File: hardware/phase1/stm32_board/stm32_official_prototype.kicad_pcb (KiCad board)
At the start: 6 copper layers, 77 parts, among them CN11 Conn_02x36_Odd_Even, CN12 Conn_02x36_Odd_Even, CN14 USB_B_Micro, CN5 Conn_ARM_JTAG_SWD_10, T2 9013, U11 STM32L496ZGTx, U13 USBLC6-2SC6, U8 TSV631AILT, U9 ESDALC6V1W5

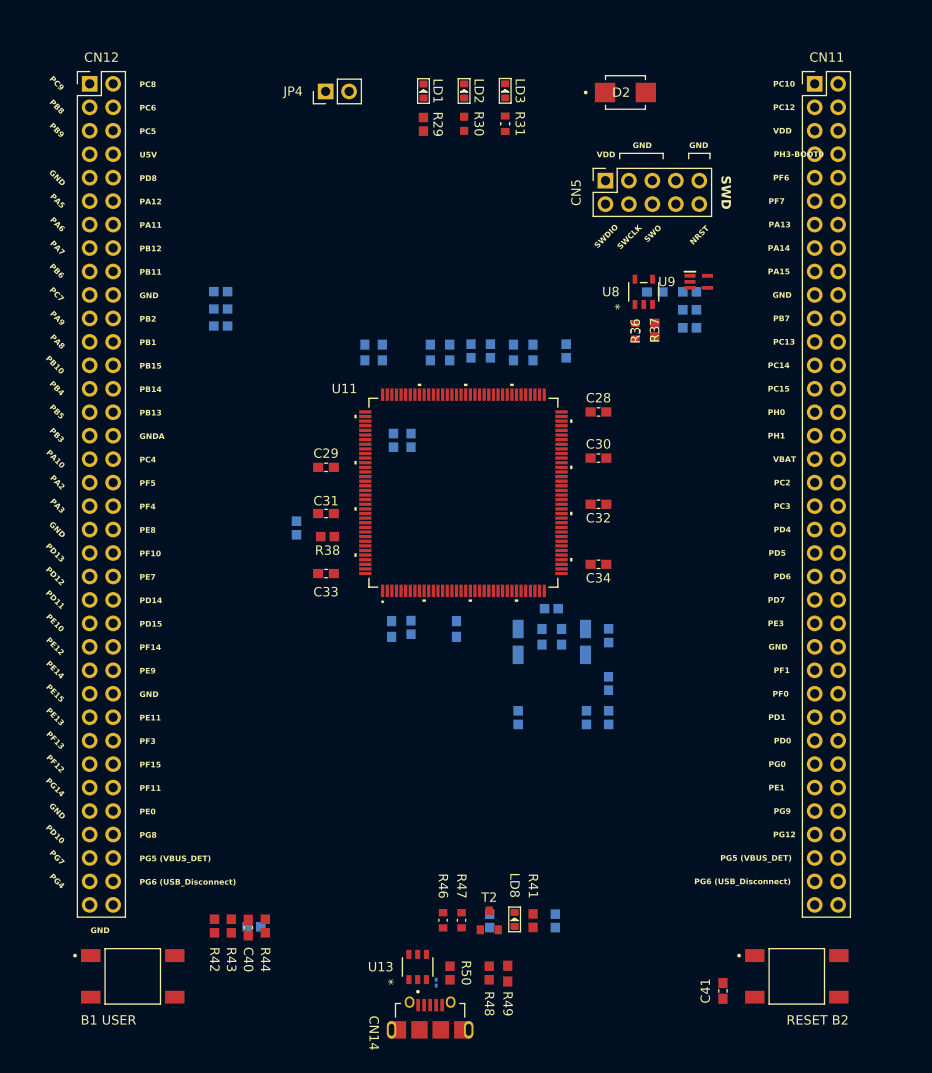
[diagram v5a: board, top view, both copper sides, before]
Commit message: toreyin meeting stm32 board update (1.29.25)
- I MUST NOT FORGET DIFFERENTIAL ROUTING FOR USB
- i need like 10 pins to wire, difficult at this point to get through the entire spider web of traces
- buttons, USB, LEDs, and power network need to be connected to main circuit
- we for sure ordering this week
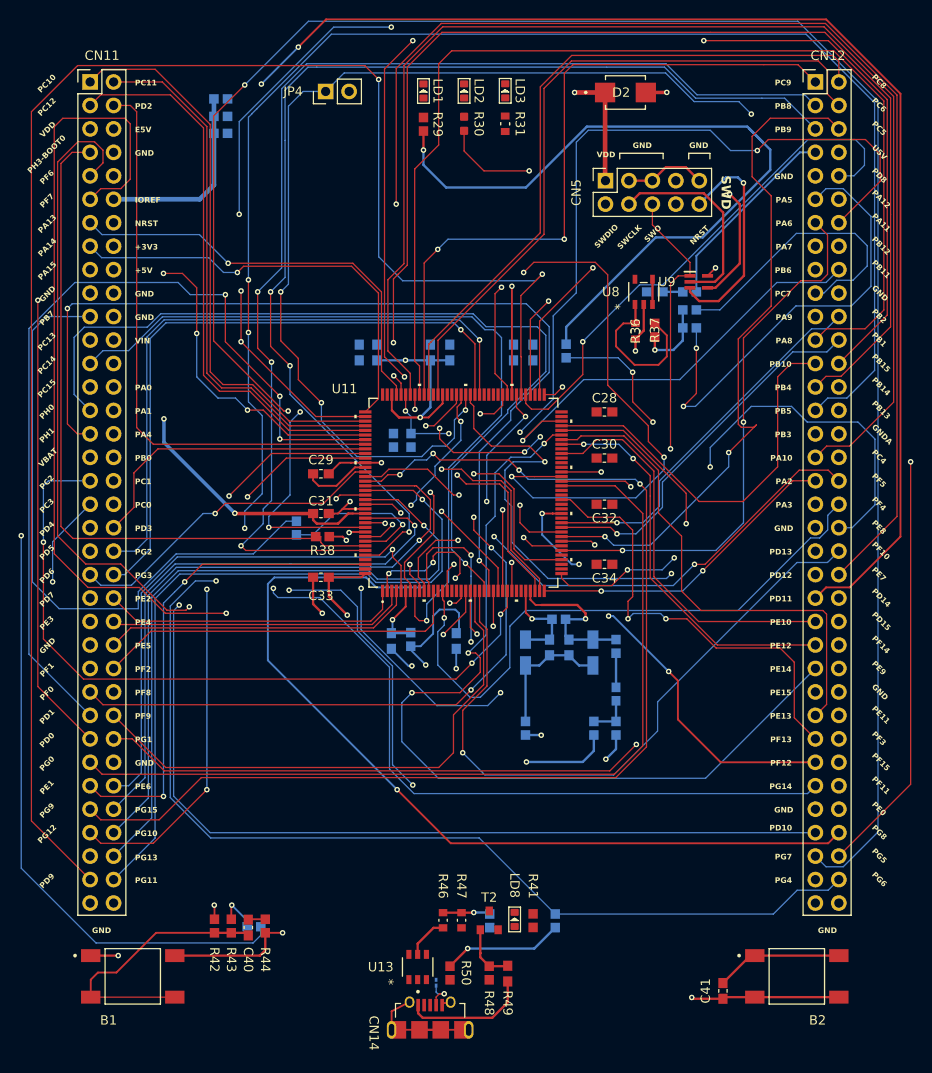
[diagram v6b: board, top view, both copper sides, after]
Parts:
- removed SB130, SB131: Closed, RC0603JR-070RL:RESC1607X60N
- B1: renamed from B1 USER
- B2: renamed from RESET B2
- moved CN12 78.6 mm to (171.4, 38.3)
- moved CN11 78.5 mm to (92.5, 38.3)
- moved SB111 20.9 mm to (103.6, 43.8)
- moved SB110 20.9 mm to (103.6, 40.1)
- moved SB112 20.9 mm to (103.6, 42.0)
- moved C58 1.40 mm to (141.3, 99.5)
- moved SB152 1.40 mm to (146.4, 99.4)
- moved SB158 1.40 mm to (144.0, 108.2)
- moved SB167 1.40 mm to (146.4, 108.2)
- moved C59 1.40 mm to (143.9, 100.0)
- moved L3 1.40 mm to (146.4, 104.5)
- moved C57 1.40 mm to (139.2, 99.5)
- moved SB149 1.40 mm to (140.2, 96.5)
- moved SB166 1.40 mm to (136.6, 108.2)
- moved C56 1.40 mm to (136.6, 100.0)
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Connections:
- R30 pad 1: Net-(R30-Pad1) -> PB7
- SB172 pad 1: PB7 -> Net-(U11-PB7)
- SB172 pad 2: Net-(R30-Pad1) -> PB7
- U11 pad 137: PB7 -> Net-(U11-PB7)
- U9 pad 5: (no net) -> GND
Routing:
- net PG7: track 0.00 -> 224.1 mm, vias 0 -> 3
- net VDD: track 0.00 -> 223.4 mm, vias 0 -> 6
- net PG5 (VBUS_DET): track 0.00 -> 208.0 mm, vias 0 -> 5
- net PE7: track 0.00 -> 204.6 mm, vias 0 -> 4
- net PD12: track 0.00 -> 193.4 mm, vias 0 -> 3
- net PD11: track 0.00 -> 188.4 mm, vias 0 -> 3
- net PD9: track 0.00 -> 178.4 mm, vias 0 -> 2
- net NRST: track 0.00 -> 176.5 mm, vias 0 -> 2
- net PB5: track 0.00 -> 171.0 mm, vias 0 -> 4
- net PD13: track 0.00 -> 166.2 mm, vias 0 -> 3
- net PB4: track 0.00 -> 162.1 mm, vias 0 -> 3
- net PB3: track 0.00 -> 157.2 mm, vias 0 -> 4
- net PG6 (USB_Disconnect): track 0.00 -> 149.1 mm, vias 0 -> 3
- net PD10: track 0.00 -> 146.7 mm, vias 0 -> 3
- net PC13: track 0.00 -> 146.0 mm, vias 0 -> 2
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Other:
- board text added: "+3V3"
- board text added: "+5V"
- board text added: "E5V"
- board text added: "IOREF"
- board text added: "PA0"
- board text added: "PA1"
- board text added: "PA4"
- board text added: "PB0"
- board text added: "PC0"
- board text added: "PC1"
- board text added: "PC11"
- board text added: "PD2"
- board text added: "PD3"
- board text added: "PD9"
- board text added: "PE2"
- board text added: "PE4"
- board text added: "PE5"
- board text added: "PE6"
- board text added: "PF2"
- board text added: "PF8"
- board text added: "PF9"
- board text added: "PG1"
- board text added: "PG10"
- board text added: "PG11"
- board text added: "PG13"
- board text added: "PG15"
- board text added: "PG2"
- board text added: "PG3"
- board text added: "PG5"
- board text added: "PG6"
- board text added: "VIN"
- board text removed: "PG5 (VBUS_DET)"
- board text removed: "PG6 (USB_Disconnect)"

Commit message: stm32 board update (2.2.25)
all...144 pins...are wired.
- still need to connect power circuitry to chip
- still need to connect USB circuitry to chip
- run by Mark Bruno tmrw --> order right away after
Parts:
- moved C30 0.50 mm to (145.2, 79.5)
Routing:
- net PD15: track 0.00 -> 135.5 mm, vias 0 -> 4
- net PD14: track 0.00 -> 132.1 mm, vias 0 -> 3
- net PE0: track 0.00 -> 96.0 mm, vias 0 -> 1
- net PF3: track 0.00 -> 75.9 mm, vias 0 -> 1
- net PF14: track 0.00 -> 66.9 mm, vias 0 -> 2
- net PF15: track 0.00 -> 66.2 mm, vias 0 -> 4
- net PE11: track 0.00 -> 56.4 mm
- net PF11: track 0.00 -> 55.6 mm, vias 0 -> 2
- net PE9: track 0.00 -> 50.0 mm, vias 0 -> 4
- net PG8: track 96.3 -> 126.2 mm, vias 1 -> 2
- net VDD_MCU: track 49.5 -> 57.2 mm
- net PG4: track 95.6 -> 101.9 mm
- net PE13: track 54.5 -> 60.8 mm
- net PE7: track 204.6 -> 198.4 mm
- net PD8: track 57.5 -> 51.9 mm
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
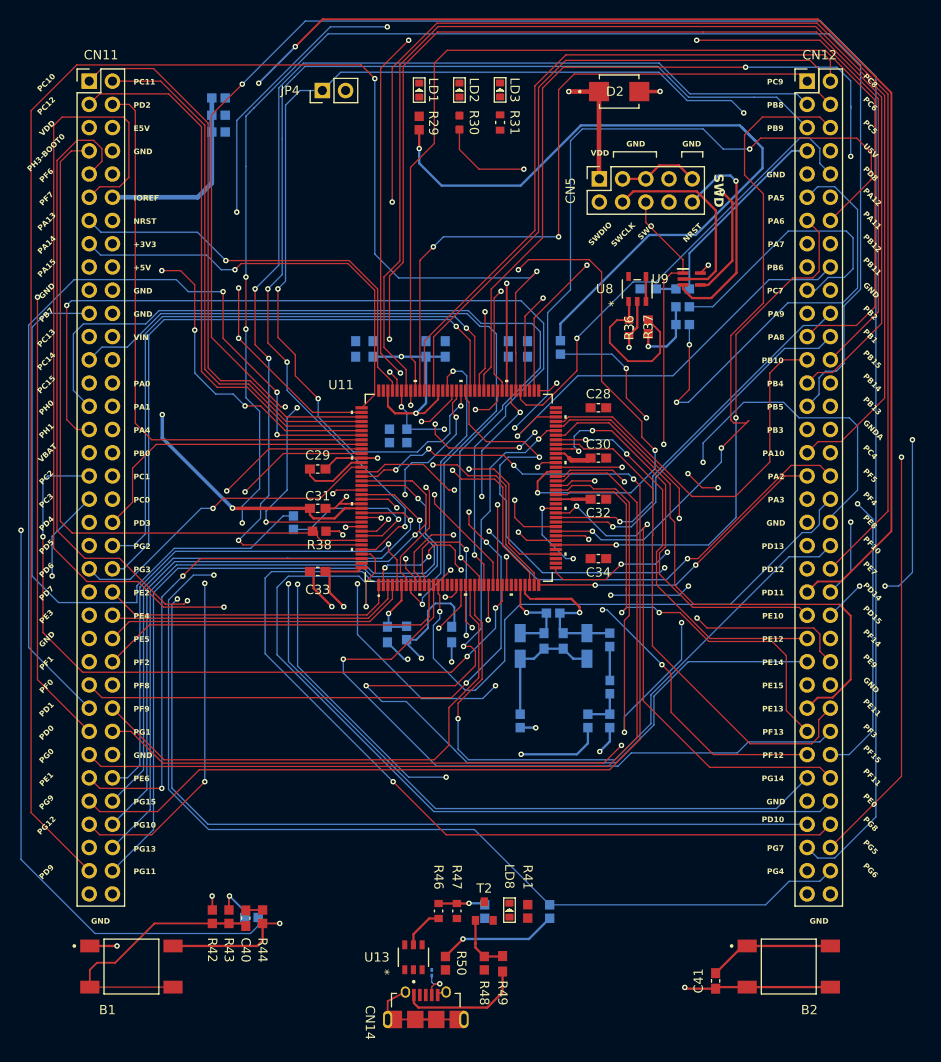
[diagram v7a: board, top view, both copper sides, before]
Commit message: layout finish, clearing all DRC errors stm32 update (2.9.25)
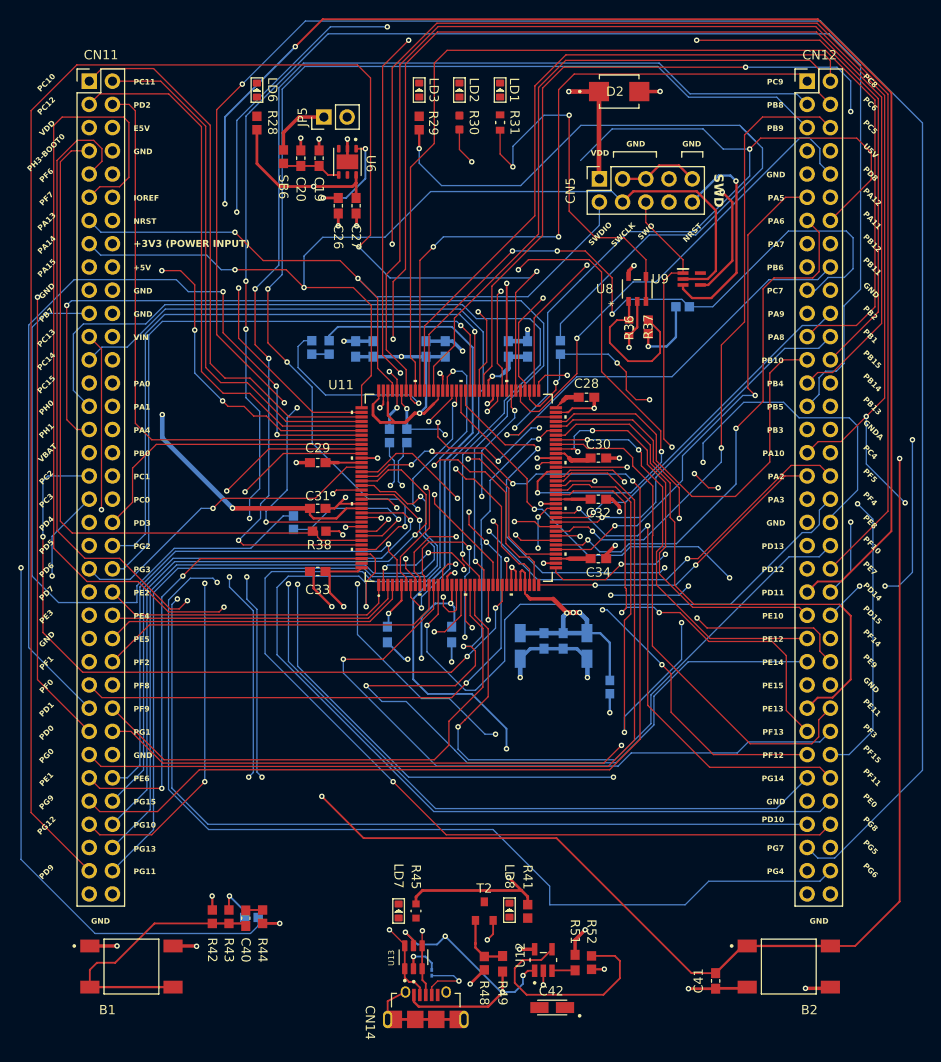
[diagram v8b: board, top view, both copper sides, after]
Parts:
- removed C45: [N/A], CC0603KRX7R7BB104:CAPC1608X90
- removed JP4: Conn_01x02_Pin, Connector_PinHeader_2.54mm:PinHeader_1x02_P2.54mm_Vertical
- removed R46: 430K, RC0603FR-07430KL:RESC1608X55N
- removed R47: 620K, RC0603FR-07620KL:RESC1608X55N
- removed R50: 1K5, RC0603FR-071K5L:RESC1607X60N
- removed SB110, SB111, SB119, SB123, SB167: Open, RC0603JR-070RL:RESC1607X60N
- removed SB112, SB149, SB152, SB154, SB158, SB166, SB199, SB201: Closed, RC0603JR-070RL:RESC1607X60N
- added C19: 1uF, CC0603KRX5R7BB105:CAPC1608X90, F.Cu at (114.6, 46.7)
- added C20: 100nF, CC0603KRX7R7BB104:CAPC1608X90, F.Cu at (112.6, 46.7)
- added C26: 100nF, CC0603KRX7R7BB104:CAPC1608X90, F.Cu at (116.7, 51.9)
- added C27: 1uF, CC0603KRX5R7BB105:CAPC1608X90, F.Cu at (118.7, 51.9)
- added C42: 4.7uF, TAJA475K016R:CAPMP3216X166, F.Cu at (140.1, 139.6)
- added JP5: Conn_01x02_Pin, Connector_PinHeader_2.54mm:PinHeader_1x02_P2.54mm_Vertical, F.Cu at (115.1, 42.2)
- added LD6: Green, SMD-LED-CLEAR-GREEN_0603_:LED-0603, F.Cu at (107.8, 39.3)
- added LD7: Red, LED-SMD-RED-DIFFUSED_0603_:LED-0603, F.Cu at (123.3, 129.0)
- added R28: 1K, RC0603FR-071KL:RESC1607X60N, F.Cu at (107.8, 42.9)
- added R45: 620, RC0603FR-07620RL:RC0603N_YAG, F.Cu at (125.2, 129.0)
- added R51: 47K, RC0603FR-0747KL:RESC1608X55, F.Cu at (142.6, 134.7)
- added R52: 10K, RC0603FR-0710KL:RESC1607X60N, F.Cu at (144.4, 134.7)
- added R54: 10K, RC0603FR-0710KL:RESC1607X60N, B.Cu at (115.7, 67.4)
- added SB135: Closed, RC0603JR-070RL:RESC1607X60N, B.Cu at (113.8, 67.4)
- added SB6: Closed, RC0603JR-070RL:RESC1607X60N, F.Cu at (110.7, 46.5)
- added U12: STMPS2151STR, STMPS2151STR:SOT95P280X145-5N, F.Cu at (139.1, 134.4)
- added U6: LD39050PU33R, LD39050PU33R:SON95P300X300X100-7N, F.Cu at (117.7, 47.1)
- U13: footprint USBLC6_2SC6:SOT23-6L_STM -> USBLC6-2SC6:SOT95P280X145-6N
- moved LD3 8.85 mm to (125.6, 39.2)
- moved LD1 8.85 mm to (134.4, 39.2)
- moved C28 1.74 mm to (143.8, 72.8)
- moved C29 0.70 mm to (114.5, 80.0), turned to 180 degrees
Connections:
- net PG5 (VBUS_DET) renamed PG5
- net PG6 (USB_Disconnect) renamed PG6
- net USB_DM renamed USB_DN
- B1 pad 2: VDD_MCU -> VDD
- B1 pad 3: VDD_MCU -> VDD
- C28 pad 1: VDD_MCU -> VDD
- C29 pad 1: VDD_MCU -> VDD
- C30 pad 1: VDD_MCU -> VDD
- C32 pad 1: VDD_MCU -> VDD
- C33 pad 1: VDD_MCU -> VDD
- C34 pad 1: VDD_MCU -> VDD
- C49 pad 1: VDD_MCU -> VDD
- C53 pad 1: VDD_MCU -> VDD
- C54 pad 1: VDD_MCU -> VDD
- C56 pad 1: VREF+ -> AVDD
- C56 pad 2: GNDA -> GND
- C57 pad 1: VREF+ -> AVDD
- C57 pad 2: GNDA -> GND
- C58 pad 2: GNDA -> GND
- C59 pad 2: GNDA -> GND
- C60 pad 1: VBAT -> VDD
- C61 pad 1: VDD_MCU -> VDD
- CN11 pad 33: VBAT -> VDD
- CN12 pad 32: GNDA -> GND
- CN12 pad 7: Net-(CN12-Pin_7) -> (no net)
- CN14 pad 1: PA9 -> USB_VBUS
- L3 pad 1: Net-(L3-Pad1) -> VDD
- L3 pad 2: Net-(L3-Pad2) -> AVDD
- R41 pad 2: +3V3_PER -> VDD
- R44 pad 1: VDD_MCU -> VDD
- R49 pad 1: PA9 -> USB_VBUS
- U11 pad 108: VDD_MCU -> VDD
- U11 pad 121: VDD_MCU -> VDD
- U11 pad 144: VDD_MCU -> VDD
- U11 pad 17: VDD_MCU -> VDD
- U11 pad 30: GNDA -> GND
- U11 pad 31: GNDA -> GND
- U11 pad 32: VREF+ -> AVDD
- U11 pad 39: VDD_MCU -> VDD
- U11 pad 52: VDD_MCU -> VDD
- U11 pad 6: VBAT -> VDD
- U11 pad 62: VDD_MCU -> VDD
- U11 pad 72: VDD_MCU -> VDD
- U11 pad 84: VDD_MCU -> VDD
- U13 pad 5: PA9 -> USB_VBUS
- U8 pad 5: +3V3_PER -> VDD
- U9 pad 5: GND -> (no net)
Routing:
- net NRST: track 176.5 -> 342.3 mm, vias 2 -> 4
- net USB_VBUS: track 0.00 -> 129.0 mm, vias 0 -> 5
- net PG5: track 208.0 -> 81.1 mm, vias 5 -> 2
- net PA10: track 142.8 -> 249.6 mm, vias 1 -> 3
- net USB_DN: track 0.00 -> 86.1 mm, vias 0 -> 4
- net VDD: track 223.6 -> 308.5 mm, vias 6 -> 18
- net USB_DP: track 0.00 -> 83.7 mm, vias 0 -> 4
- net VDD_MCU: track 57.2 -> 0.00 mm, vias 5 -> 0
- net GND: track 62.9 -> 118.9 mm, vias 12 -> 43
- net PC7: track 31.0 -> 75.6 mm, vias 0 -> 3
- net +3V3: track 0.00 -> 42.9 mm, vias 0 -> 1
- net PA14: track 69.5 -> 109.1 mm, vias 1 -> 2
- net Net-(U8-IN-): track 2.73 -> 40.1 mm, vias 0 -> 2
- net PA13: track 73.0 -> 105.4 mm, vias 2 -> 3
- net Net-(U12-EN): track 0.00 -> 24.5 mm
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- added copper zone on In4.Cu, net GND
- added copper zone on In3.Cu, net VDD
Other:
- rule pad_to_mask_clearance: 0.038 -> 0
- board text added: "+3V3 (POWER INPUT)"
- board text removed: "+3V3"
